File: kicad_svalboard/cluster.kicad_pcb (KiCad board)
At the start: 2 copper layers, 24.5 x 36.5 mm, 17 parts, among them J1 Conn_01x07, Q1 E6QYDD1204-PRA, Q2 E6QYDD1204-PRA, Q3 E6QYDD1204-PRA, Q4 E6QYDD1204-PRA, Q5 E6QYDD1204-PRA

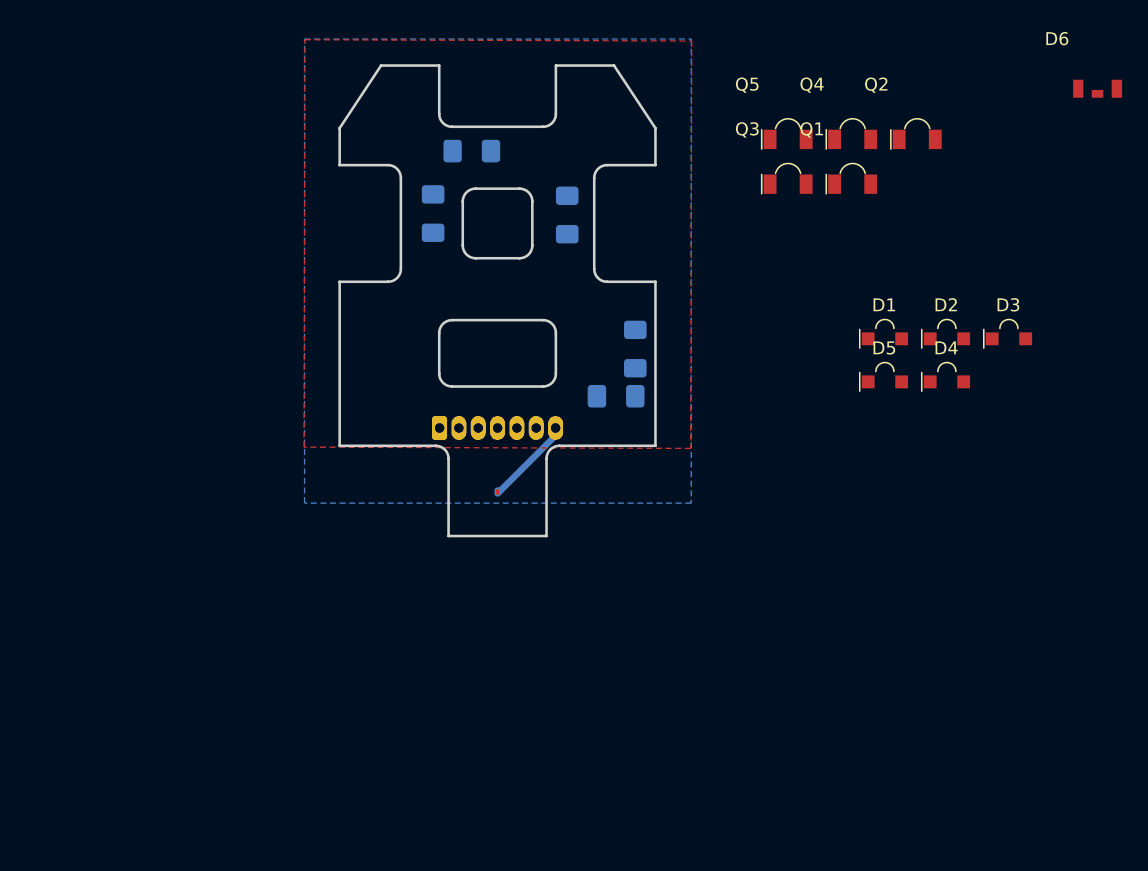
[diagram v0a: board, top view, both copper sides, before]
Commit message: Removed datasheets folder, updated design with layouts for cluster and main PCB.  still need FFC connectors on main PCB
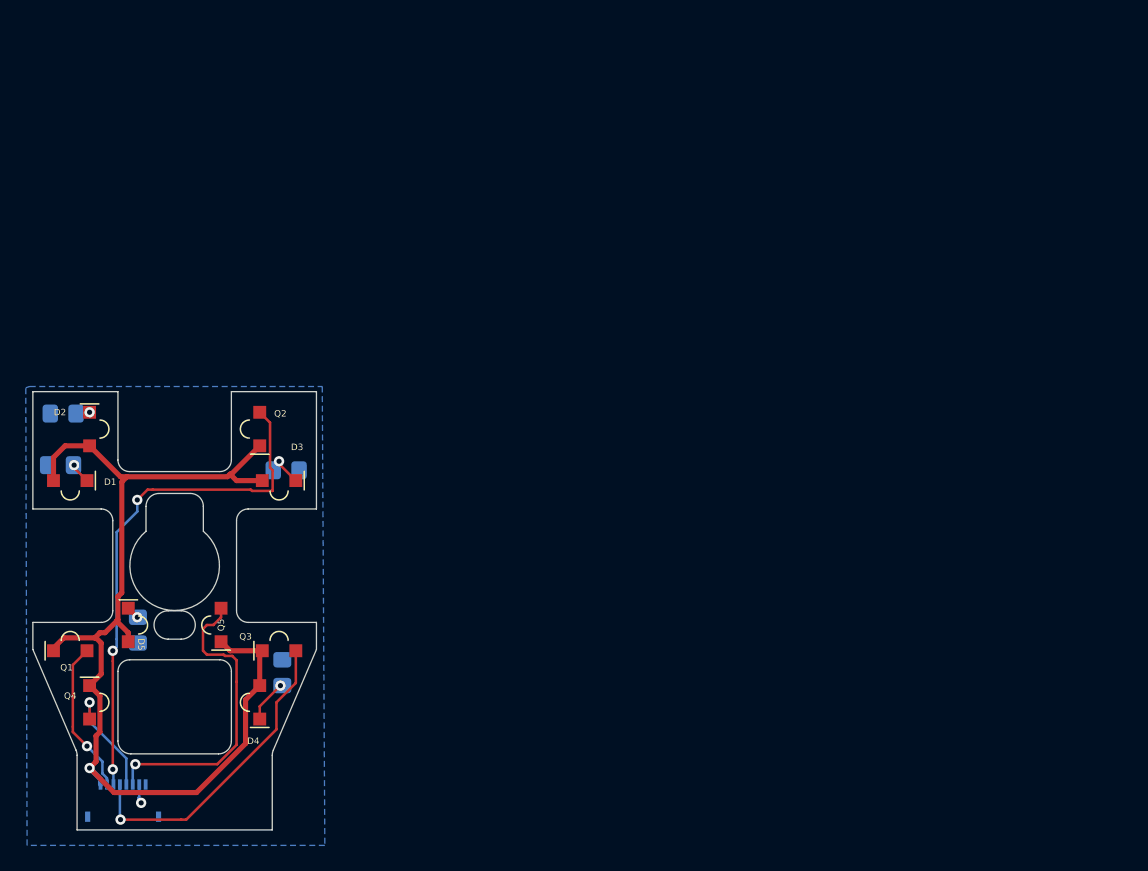
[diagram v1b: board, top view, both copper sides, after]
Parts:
- removed D6: PD12-21B/TR8, lalboard:PD12-21B
- D1, D2, D3, D4, D5: value IR12-21C/TR8 -> IR12-21C; footprint lalboard:IR12-21C-TR8 -> lalboard:IR12-21C
- J1: footprint lalboard:JST_ZH_S7B-ZR_1x07_P1.50mm_Horizontal -> lalboard:FH34SRJ8S05SH50
- Q1, Q2, Q3, Q4, Q5: value E6QYDD1204-PRA -> PT12-21B; footprint lalboard:E6QYDD1204-PRA -> lalboard:PT12-21B
- R1, R2, R3, R4, R5: footprint Resistor_SMD:R_1206_3216Metric_Pad1.42x1.75mm_HandSolder -> Resistor_SMD:R_0805_2012Metric_Pad1.20x1.40mm_HandSolder
- moved Q4 73.6 mm to (130.8, 112.7), turned to -90 degrees
- moved Q1 70.7 mm to (129.3, 108.7)
- moved D2 66.9 mm to (130.8, 91.5), turned to -90 degrees
- moved D1 64.2 mm to (129.3, 95.5), turned to 180 degrees
- moved D5 61.7 mm to (133.8, 106.7), turned to -90 degrees
- moved D4 58.8 mm to (144.0, 112.7), turned to 90 degrees
- moved Q5 57.9 mm to (141.0, 106.7), turned to 90 degrees
- moved D3 57.7 mm to (145.5, 95.5), turned to 180 degrees
- moved Q2 55.7 mm to (144.0, 91.5), turned to 90 degrees
- moved Q3 53.6 mm to (145.5, 108.7)
- moved R5 44.3 mm to (134.6, 107.1)
- moved R4 43.1 mm to (145.8, 110.4), turned to -90 degrees
- moved R2 42.9 mm to (128.8, 90.3), turned to 0 degrees
- moved J1 38.1 mm to (133.4, 120.6), turned to 180 degrees
- moved R1 34.9 mm to (128.6, 94.3), turned to 0 degrees
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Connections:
- Q1 pad 1: C1 -> +5V
- Q1 pad 2: +5V -> C1
- Q2 pad 1: C2 -> +5V
- Q2 pad 2: +5V -> C2
- Q3 pad 1: C3 -> +5V
- Q3 pad 2: +5V -> C3
- Q4 pad 1: C4 -> +5V
- Q4 pad 2: +5V -> C4
- Q5 pad 1: C5 -> +5V
- Q5 pad 2: +5V -> C5
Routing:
- net +5V: track 0.00 -> 81.1 mm, vias 0 -> 1
- net C2: track 0.00 -> 40.3 mm, vias 0 -> 3
- net C3: track 0.00 -> 24.5 mm, vias 0 -> 1
- net C5: track 0.00 -> 23.8 mm, vias 0 -> 1
- net C1: track 0.00 -> 11.9 mm, vias 0 -> 1
- net C4: track 0.00 -> 8.86 mm, vias 0 -> 1
- net GND: track 6.69 -> 1.53 mm, vias 0 -> 1
- net Net-(D4-Pad2): track 0.00 -> 3.41 mm, vias 0 -> 1
- net Net-(D3-Pad2): track 0.00 -> 2.92 mm, vias 0 -> 1
- net Net-(D1-Pad2): track 0.00 -> 1.66 mm, vias 0 -> 1
- net Net-(D2-Pad2): track 0.00 -> 1.09 mm, vias 0 -> 1
- net Net-(D5-Pad2): track 0.00 -> 1.04 mm, vias 0 -> 1
- removed copper zone on F.Cu, net +5V
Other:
- board size 24.5 x 36.5 mm -> 22 x 34 mm
- board text removed: "Coords for import: (150, 100)"
- board text removed: "finger cluster v0.1"
- board text removed: "lalboard.com"
